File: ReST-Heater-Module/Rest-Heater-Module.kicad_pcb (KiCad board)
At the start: 2 copper layers, 29 x 34 mm, 14 parts, among them P1 02X10-MALE, P3 02-SCREW-TERM, P4 01X02-MALE, P5 02-SCREW-TERM, Q1 Q_BSH105, Q2 Q_AOT240L

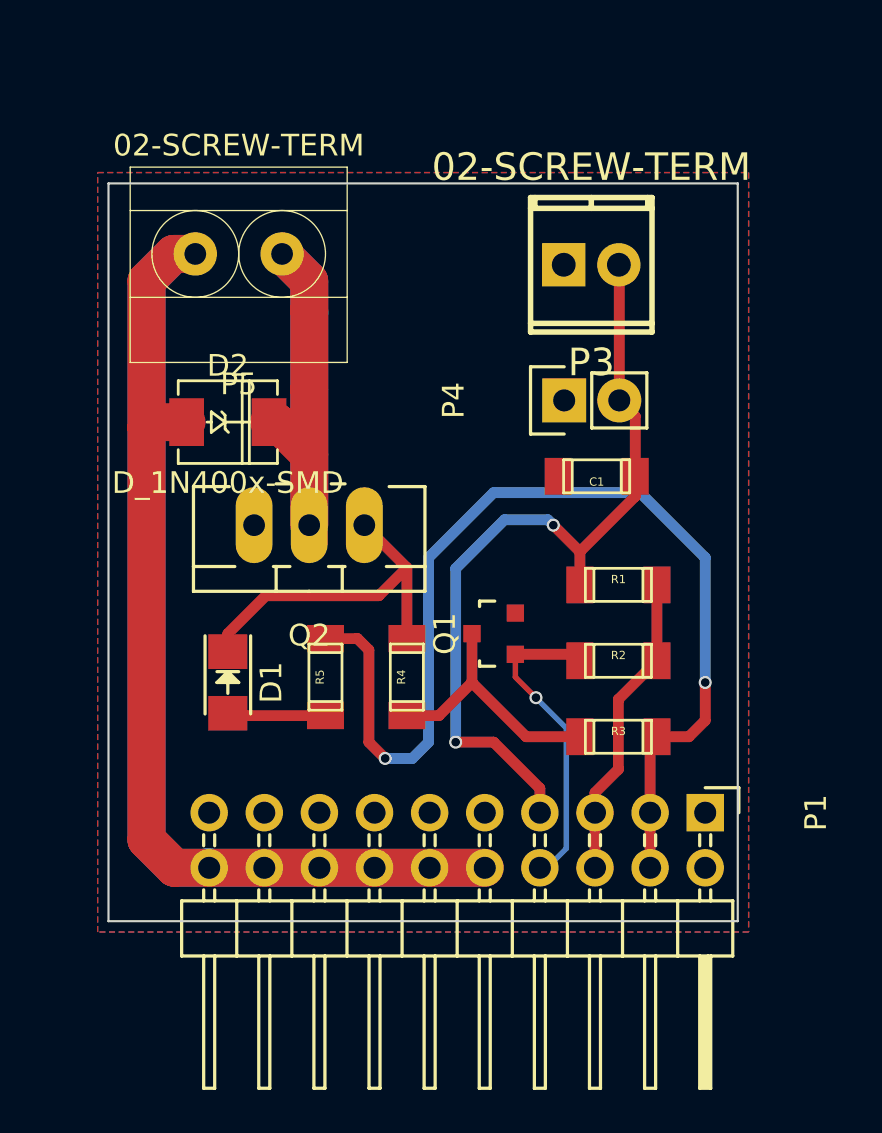
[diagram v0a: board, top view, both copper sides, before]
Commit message: PRE-RELEASE Rev. A!
Yay. I managed to finish the Main PCB over the night, must say, Im happy with it. Things that changed since the last release:

Heater:
-Heater Module uses less Pins
- Much smaller Design now

Heatbed & Additional Module: 
-Changed distance from Edge to first Pin from 2.5mm to 2mm (will be changed on other boards too)

Mainboard:
-Added I2C Pullups 4K7
-Swapped Pins from Stepper, Heaters and Endstops around for easier PCB Design.
-Finished Design (10cm x 10cm!)

Added some 3D Models for testing. If someone has problems with loading some modules, please contact me! (or make a pull request with a better solution)
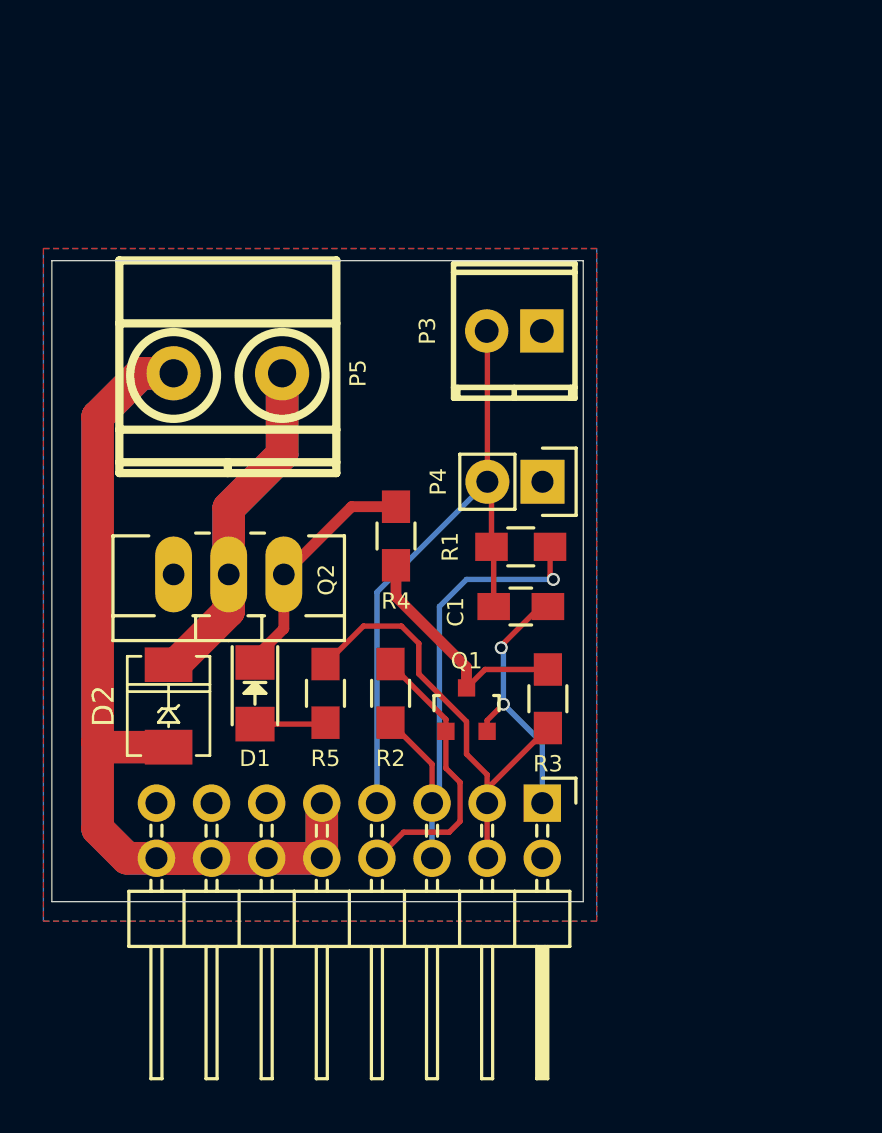
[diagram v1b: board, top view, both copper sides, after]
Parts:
- C1: value 10uF -> (none); footprint ok-smd-generic:1206 -> Capacitors_SMD:C_0805_HandSoldering
- D1: value LED -> (none)
- D2: value D_1N400x-SMD -> (none); footprint DO-214AC(SMA):DO-214AC(SMA) -> ReST-Library:DO-214AC(SMA)
- P1: value 02X10-MALE -> (none); footprint Pin_Headers:Pin_Header_Angled_2x10 -> Pin_Headers:Pin_Header_Angled_2x08
- P3: value 02-SCREW-TERM -> (none); footprint 2:mpt_0,5%2f2-2,54 -> ReST-Library:screw-2,54-2P
- P4: value 01X02-MALE -> (none)
- P5: value 02-SCREW-TERM -> (none); footprint 5mm-pitch-terminal:mkds_1,5-2 -> ReST-Library:screw-5-2P
- Q1: value Q_BSH105 -> (none)
- Q2: value Q_AOT240L -> (none)
- R1: value 4.7K -> (none); footprint ok-smd-generic:1206 -> Resistors_SMD:R_0805_HandSoldering
- R2, R3: value 100K -> (none); footprint ok-smd-generic:1206 -> Resistors_SMD:R_0805_HandSoldering
- R4: value 22R -> (none); footprint ok-smd-generic:1206 -> Resistors_SMD:R_0805_HandSoldering
- R5: value 470R -> (none); footprint ok-smd-generic:1206 -> Resistors_SMD:R_0805_HandSoldering
- moved D2 13.4 mm to (138.3, 125.6), turned to 90 degrees
- moved R2 10.6 mm to (148.5, 125.0), turned to 270 degrees
- moved P1 7.52 mm to (155.5, 130.1)
- moved C1 6.95 mm to (154.5, 121.0), turned to 0 degrees
- moved R4 6.52 mm to (148.8, 117.8)
- moved P5 5.52 mm to (141.0, 110.2), turned to 0 degrees
- moved R1 4.83 mm to (154.5, 118.2)
- moved P3 4.68 mm to (154.2, 108.3), turned to 0 degrees
- moved Q2 4.35 mm to (141.0, 119.5)
- moved P4 3.88 mm to (155.5, 115.2), turned to 270 degrees
- moved Q1 3.72 mm to (152.0, 125.8), turned to 0 degrees
- moved R3 3.69 mm to (155.8, 125.2), turned to 270 degrees
- moved D1 1.35 mm to (142.2, 125.0)
- moved R5 0.75 mm to (145.5, 125.0)
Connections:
- P1 pad 9: GND -> +12V
- P5 pad 1: Net-(D2-Pad2) -> +12V
- P5 pad 2: +12V -> Net-(D2-Pad2)
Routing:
- net +5V: track 49.8 -> 21.2 mm, vias 2 -> 0
- net GND: track 0.00 -> 12.5 mm, vias 0 -> 2
- net +12V: track 91.3 -> 79.4 mm
- net +3V3: track 14.2 -> 23.6 mm, vias 0 -> 1
- net /T1: track 37.3 -> 29.8 mm, vias 2 -> 0
- net Net-(D1-Pad1): track 16.5 -> 11.1 mm
- net Net-(D2-Pad2): track 28.7 -> 26.1 mm
- net Net-(D1-Pad2): track 5.05 -> 3.28 mm
- net /PWM-HEATER: track 14.6 -> 13.1 mm, vias 1 -> 0
- net Net-(Q1-Pad3): track 11.9 -> 11.1 mm
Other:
- board size 29 x 34 mm -> 24.5 x 29.5 mm

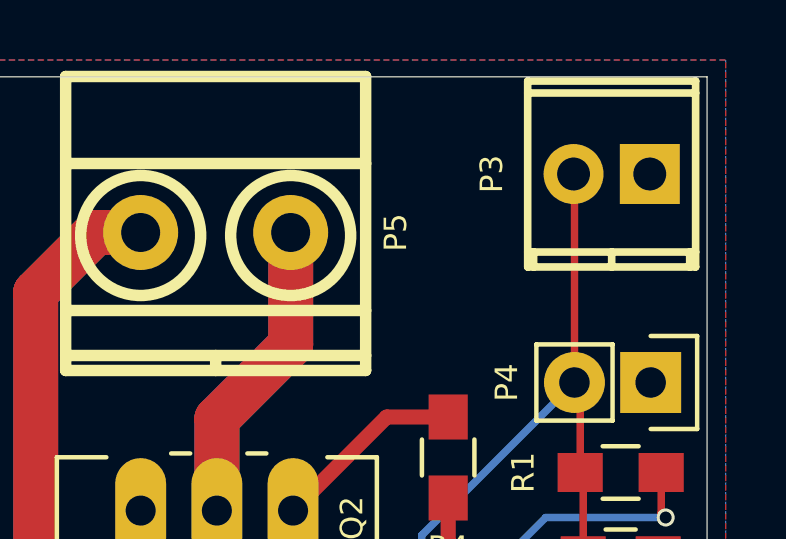
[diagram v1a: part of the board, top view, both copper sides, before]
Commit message: Added Images and PDF's
+ Silkscreening
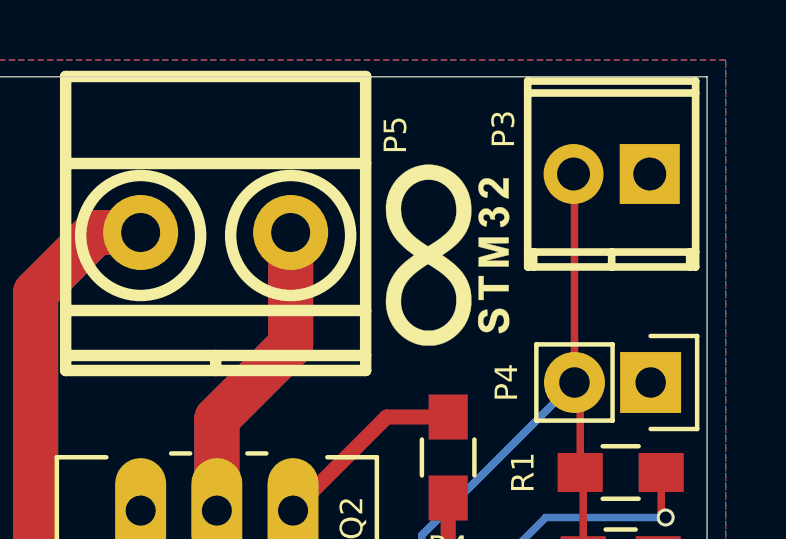
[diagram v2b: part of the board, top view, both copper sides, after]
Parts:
- added G***: LOGO, ReST-Library:Logo_silk_OSHW_6x6mm, B.Cu at (147.8, 114.2)
- added G***: LOGO, ReST-Library:STM32, F.Cu at (148.8, 111.0)
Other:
- board text added: "ReST32 Heater Rev. A | Test PCB by Straw"

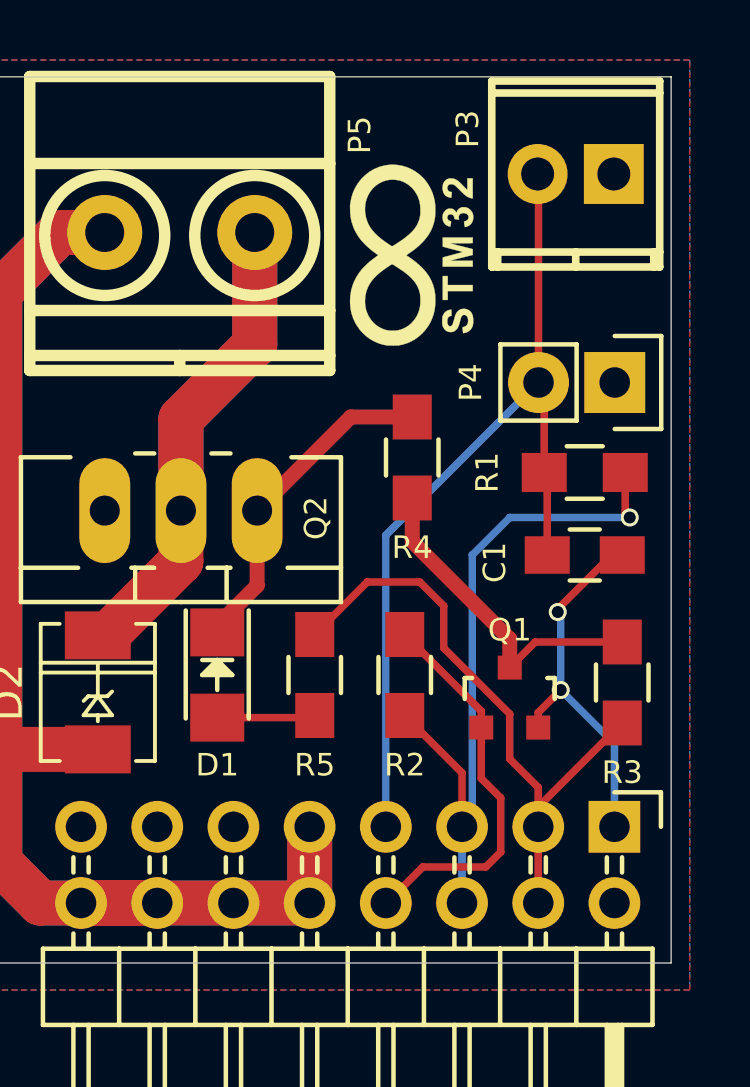
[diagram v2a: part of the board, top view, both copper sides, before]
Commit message: Added Mounting Holes to all Modules
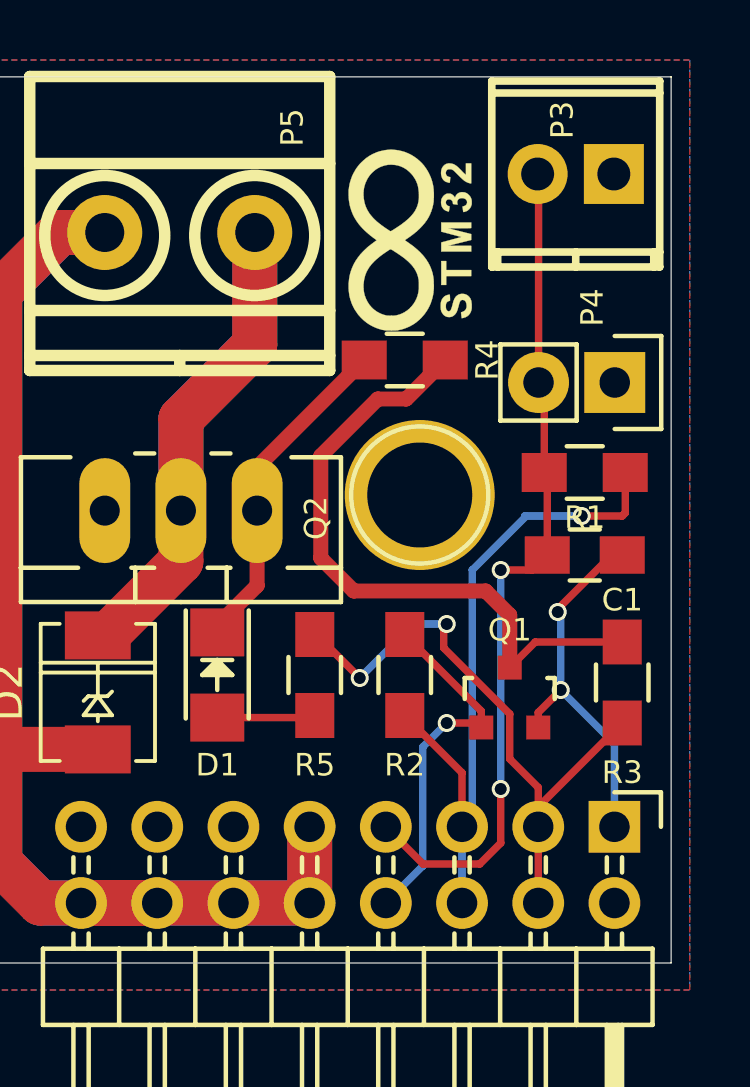
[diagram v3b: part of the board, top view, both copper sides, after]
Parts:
- added ?: 1pin, Connect:1pin, F.Cu at (149.0, 119.0)
- moved R4 3.26 mm to (148.5, 114.5), turned to 180 degrees
- moved G*** 1.77 mm to (148.7, 112.7)
- moved G*** 0.50 mm to (148.8, 110.5)
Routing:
- net Net-(Q1-Pad3): track 11.1 -> 21.8 mm
- net /T1: track 29.8 -> 28.4 mm, vias 0 -> 2
- net Net-(D1-Pad1): track 11.1 -> 12.3 mm
- net /PWM-HEATER: track 13.1 -> 12.2 mm, vias 0 -> 1
- net +5V: track 21.2 -> 21.0 mm, vias 0 -> 2
